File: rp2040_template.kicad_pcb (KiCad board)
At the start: 2 copper layers, 37 parts, among them J1 USB_C_Receptacle_USB2.0_14P, J3 SWD, SW1 SW_BOOT, SW2 SW_RESET, U1 RP2040, U2 W25Q16JVUXIQ TR, U3 AP2202K-3.3TRG1, Y1 ABM8-272-T3

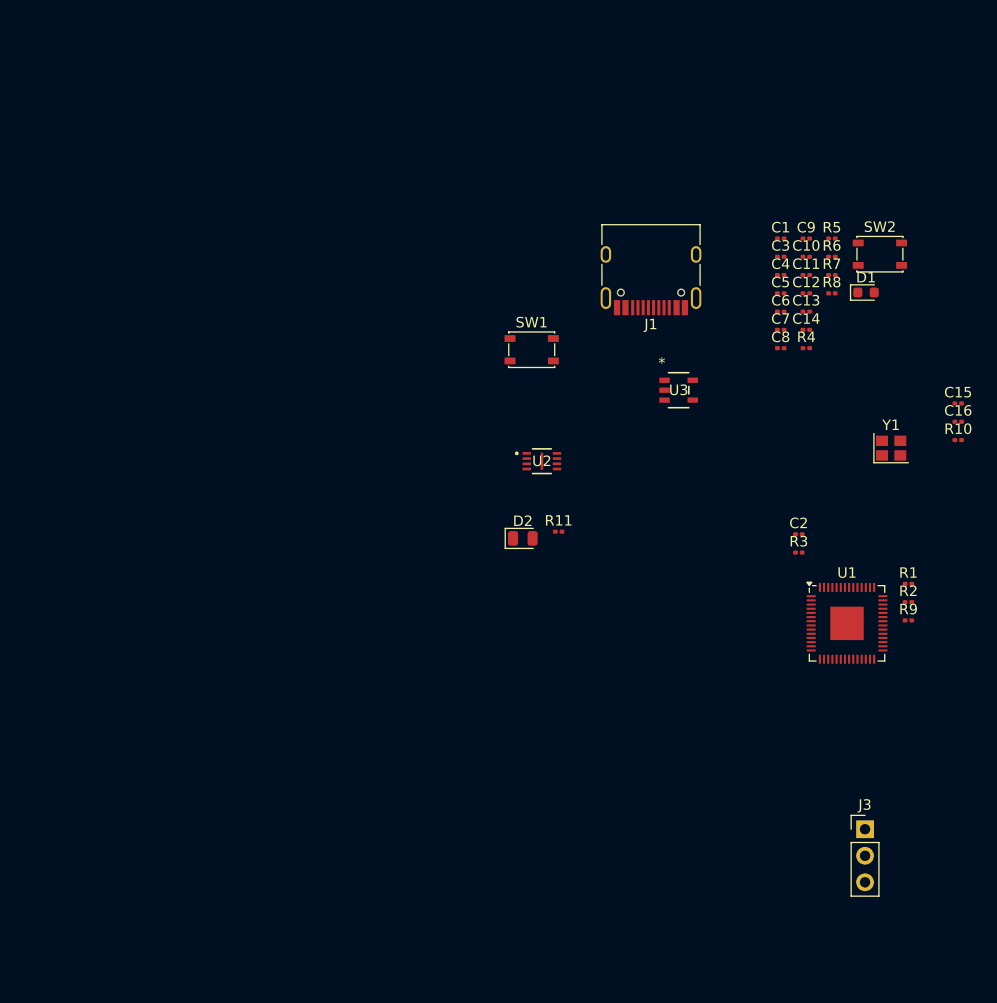
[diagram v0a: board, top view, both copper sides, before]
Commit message: Added castellated edges to PCB. began work on layout.
Signed-off-by: Nate <natelostintimeandspace@gmail.com>
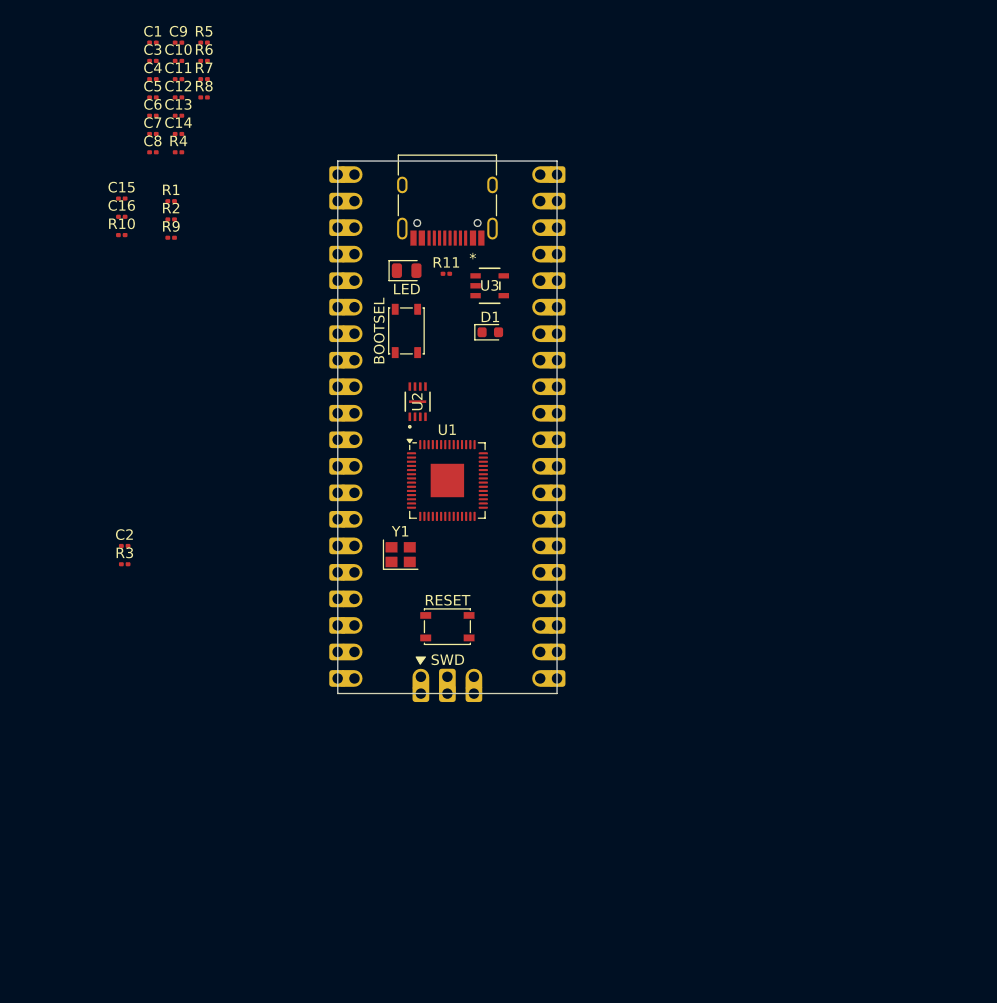
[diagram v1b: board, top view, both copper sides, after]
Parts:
- removed J3: SWD, Connector_PinHeader_2.54mm:PinHeader_1x03_P2.54mm_Vertical
- added REF**: castellated_tht_1x20, castellated:castellated_tht_1x20, F.Cu at (119.4, 51.3)
- added REF**: castellated_tht_1x20, castellated:castellated_tht_1x20, F.Cu at (101.6, 99.6)
- added REF**: castellated_tht_1x3, castellated:castellated_tht_1x3, F.Cu at (113.0, 99.4)
- moved C15 82.5 mm to (79.3, 53.6)
- moved C16 82.5 mm to (79.3, 55.3)
- moved R10 82.5 mm to (79.3, 57.1)
- moved R1 79.6 mm to (84.0, 53.8)
- moved R2 79.6 mm to (84.0, 55.6)
- moved R9 79.6 mm to (84.0, 57.3)
- moved C2 64.6 mm to (79.6, 86.9)
- moved R3 64.6 mm to (79.6, 88.6)
- moved C1 63.0 mm to (82.3, 38.7)
- moved C10 63.0 mm to (84.7, 40.4)
- moved C11 63.0 mm to (84.7, 42.2)
- moved C12 63.0 mm to (84.7, 43.9)
- moved C13 63.0 mm to (84.7, 45.7)
- moved C14 63.0 mm to (84.7, 47.4)
- moved C3 63.0 mm to (82.3, 40.4)
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- renumbered SW1 to BOOTSEL, D2 to LED, SW2 to RESET
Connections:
- U1 pad 24: /SWCLK -> unconnected-(U1-SWCLK-Pad24)
- U1 pad 25: /SWDIO -> unconnected-(U1-SWD-Pad25)
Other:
- board outline added: 21 x 51 mm

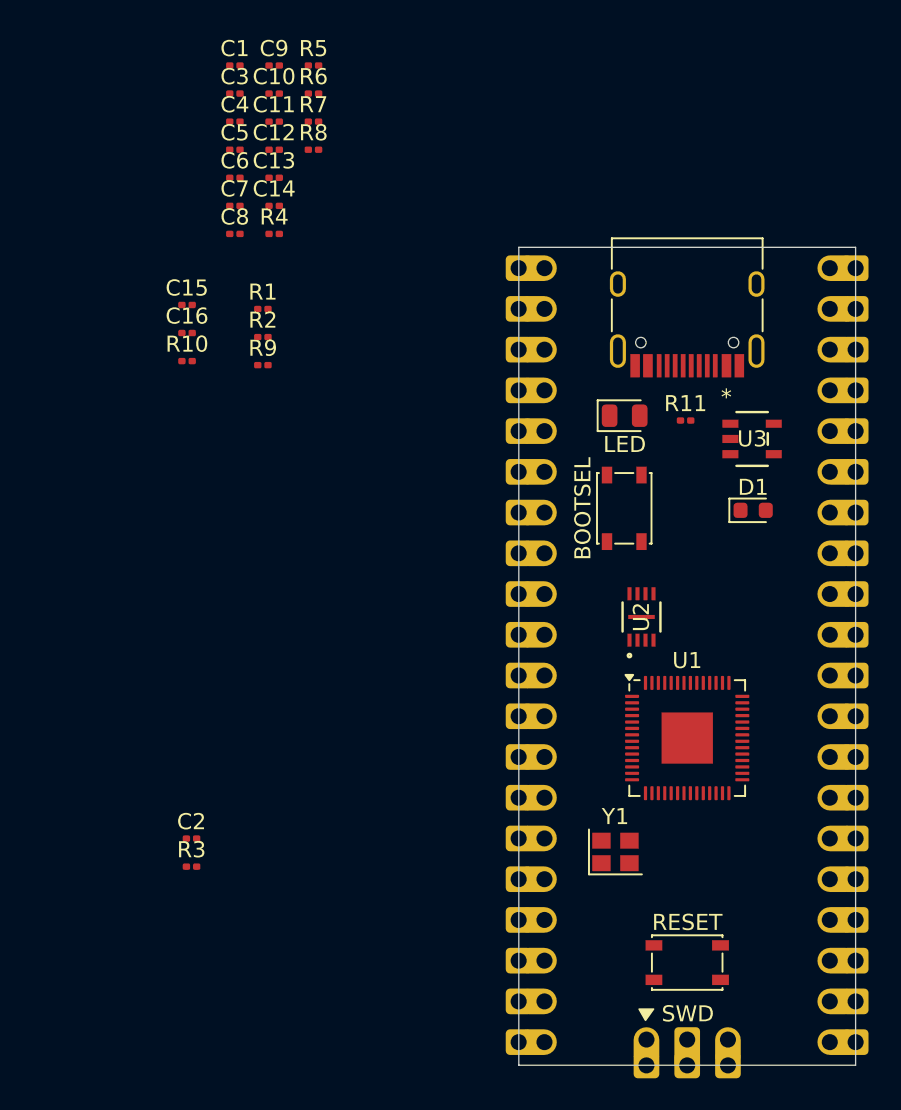
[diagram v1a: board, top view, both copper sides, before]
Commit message: Routed USB data, Oscillator, and began QSPI layout.
Signed-off-by: Nate <natelostintimeandspace@gmail.com>
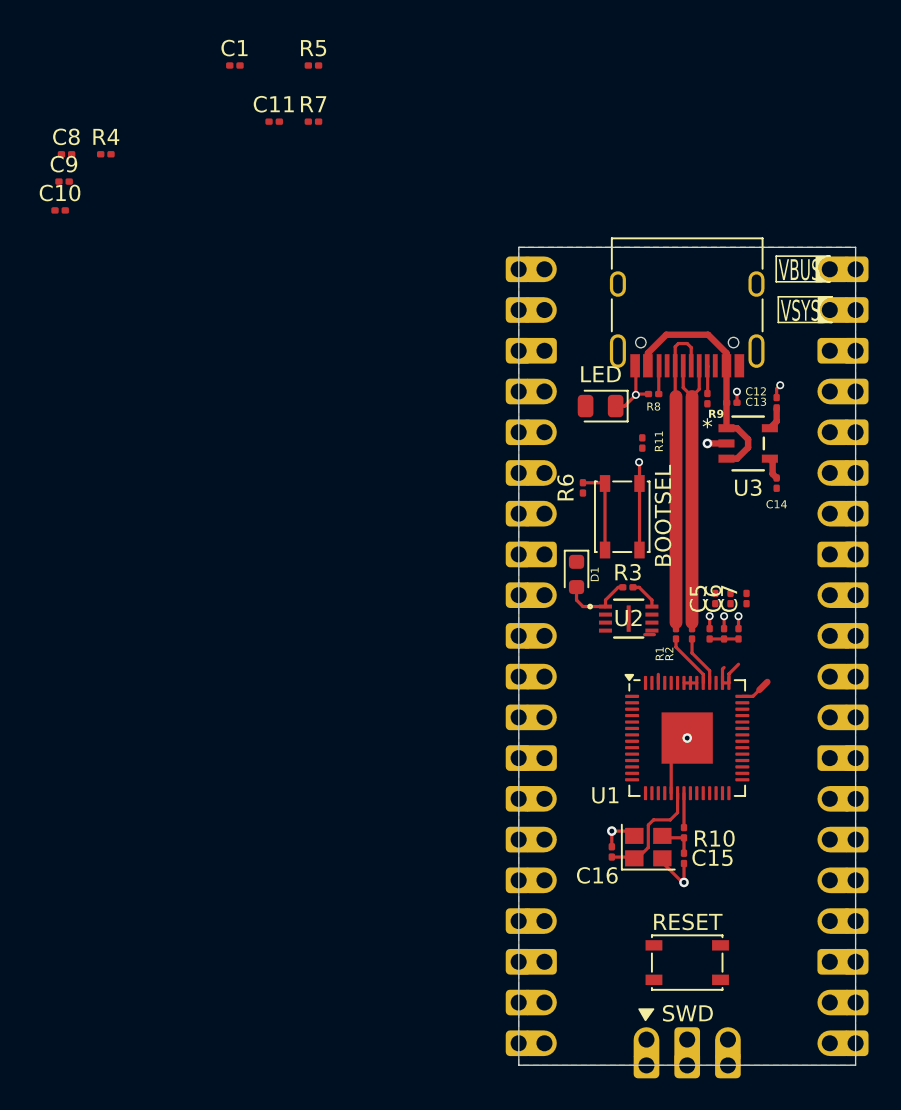
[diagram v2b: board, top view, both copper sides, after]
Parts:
- moved C15 46.4 mm to (110.3, 88.1), turned to 90 degrees
- moved C3 45.4 mm to (112.8, 74.1), turned to 90 degrees
- moved C4 44.8 mm to (113.7, 74.1), turned to 90 degrees
- moved R10 42.7 mm to (110.3, 86.5), turned to 90 degrees
- moved C16 41.8 mm to (105.8, 87.7), turned to -90 degrees
- moved C5 41.0 mm to (112.2, 71.9), turned to 90 degrees
- moved C6 40.5 mm to (113.2, 71.9), turned to 90 degrees
- moved C7 40.2 mm to (114.2, 71.9), turned to 90 degrees
- moved C14 35.8 mm to (116.1, 64.7), turned to -90 degrees
- moved C2 34.7 mm to (111.9, 74.1), turned to 90 degrees
- moved C13 34.3 mm to (116.1, 59.7), turned to 90 degrees
- moved R1 32.8 mm to (109.8, 74.1), turned to -90 degrees
- moved C12 32.6 mm to (113.3, 59.7)
- moved R2 32.5 mm to (110.8, 74.1), turned to -90 degrees
- moved R3 32.3 mm to (106.8, 71.2), turned to 180 degrees
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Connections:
- REF** pad 1: (no net) -> GND (x2)
- REF** pad 2: (no net) -> GND (x2)
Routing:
- net GND: track 0.00 -> 24.4 mm, vias 0 -> 11
- net USB_DP: track 0.00 -> 19.5 mm
- net USB_DM: track 0.00 -> 18.3 mm
- net VBUS: track 0.00 -> 15.1 mm
- net +3V3: track 0.00 -> 10.7 mm
- net /XIN: track 0.00 -> 7.35 mm
- net Net-(SW1-A): track 0.00 -> 5.54 mm
- net /~{QSPI_CS}: track 0.00 -> 4.59 mm
- net Net-(U1-USB_DP): track 0.00 -> 3.40 mm
- net Net-(U1-USB_DM): track 0.00 -> 3.15 mm
- net Net-(C15-Pad2): track 0.00 -> 2.36 mm
- net /XOUT: track 0.00 -> 2.14 mm
- net Net-(J1-CC1): track 0.00 -> 1.80 mm
- net Net-(J1-CC2): track 0.00 -> 1.78 mm
- net Net-(U3-BYP/ADJ): track 0.00 -> 1.38 mm
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- added copper zone on B.Cu, net GND
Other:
- board text added: "VBUS"
- board text added: "VSYS"

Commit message: Finished Rev A!
Signed-off-by: Nate <natelostintimeandspace@gmail.com>
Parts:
- removed the C2 at (111.9, 74.1)
- removed the REF** at (119.4, 51.4)
- removed the REF** at (101.6, 99.6)
- removed the REF** at (113.0, 99.4)
- removed U1: RP2040, Package_DFN_QFN:QFN-56-1EP_7x7mm_P0.4mm_EP3.2x3.2mm
- added ?: , , F.Cu at (147.5, 107.4)
- added ?: , , F.Cu at (146.2, 107.4)
- added ?: , , F.Cu at (147.5, 108.7)
- added ?: , , F.Cu at (148.8, 107.4)
- added ?: , , F.Cu at (146.2, 108.7)
- added ?: , , F.Cu at (148.8, 108.7)
- added ?: , , F.Cu at (147.5, 106.1)
- added ?: , , F.Cu at (146.2, 106.1)
- added ?: , , F.Cu at (148.8, 106.1)
- added C17: 100nF, Capacitor_SMD:C_01005_0402Metric, F.Cu at (152.4, 108.5)
- added C2: 100nF, Capacitor_SMD:C_0201_0603Metric, F.Cu at (152.4, 102.8)
- added C2: 100nF, Capacitor_SMD:C_01005_0402Metric, F.Cu at (146.7, 94.6)
- added D3: D_Schottky, Diode_SMD:Nexperia_CFP3_SOD-123W, F.Cu at (154.1, 79.6)
- added FID1: Fiducial, Fiducial:Fiducial_0.5mm_Mask1mm, F.Cu at (141.1, 78.0)
- added FID2: Fiducial, Fiducial:Fiducial_0.5mm_Mask1mm, F.Cu at (152.7, 125.8)
- added G***: LOGO, LOGO, B.Cu at (147.1, 120.7)
- added J2: Conn_01x20_Pin, castellated:castellated_tht_1x20, B.Cu at (138.6, 78.2)
- added J3: Conn_01x20_Pin, castellated:castellated_tht_1x20, F.Cu at (156.3, 78.2)
- added J4: Conn_01x03_Pin, castellated:castellated_tht_1x3, F.Cu at (150.0, 126.2)
- added REF**: OSHW-Logo2_7.3x6mm_SilkScreen, Symbol:OSHW-Logo2_7.3x6mm_SilkScreen, B.Cu at (145.7, 90.8)
- added U4: RP2040, Package_DFN_QFN:QFN-56-1EP_7x7mm_P0.4mm_EP3.2x3.2mm, F.Cu at (147.5, 107.4)
- C1, C10, C11, C12, C13, C14, C15, C16, C3, C4, C5, C6, C7, C8, C9: footprint Capacitor_SMD:C_0201_0603Metric -> Capacitor_SMD:C_01005_0402Metric
- D1: footprint Diode_SMD:D_0603_1608Metric -> Diode_SMD:D_01005_0402Metric
- LED1: renamed from LED; footprint LED_SMD:LED_0805_2012Metric -> LED_SMD:LED_0402_1005Metric_Pad0.77x0.64mm_HandSolder
- SW_1: renamed from BOOTSEL; value SW_BOOT -> BOOTSEL
- SW_2: renamed from RESET; value SW_RESET -> RESET
- U2: footprint footprints:USON-8_UX_2x3x0p6_WIN -> Package_SON:Winbond_USON-8-1EP_3x2mm_P0.5mm_EP0.2x1.6mm
- moved R7 96.9 mm to (150.4, 115.6)
- moved C10 95.6 mm to (150.6, 101.2), turned to 90 degrees
- moved C8 95.1 mm to (148.0, 101.1), turned to 90 degrees
- moved C9 94.4 mm to (142.4, 108.5), turned to 180 degrees
- moved C1 94.3 mm to (152.3, 101.9)
- moved C11 89.7 mm to (152.3, 101.2)
- moved R4 86.1 mm to (143.9, 94.9), turned to 180 degrees
- moved R5 79.1 mm to (143.9, 93.9)
- moved C5 54.7 mm to (147.7, 113.5), turned to -90 degrees
- moved C6 54.6 mm to (148.6, 113.5), turned to -90 degrees
- moved C13 49.3 mm to (151.7, 93.7), turned to -90 degrees
- moved Y1 48.8 mm to (145.9, 118.2)
- moved C16 48.7 mm to (145.5, 115.9), turned to 0 degrees
- moved R6 48.5 mm to (142.7, 94.2)
- moved R1 47.5 mm to (148.8, 101.2)
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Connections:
- C10 pad 1: Net-(U1-VREG_VOUT) -> +1V1
- C12 pad 1: VBUS -> /VSYS
- C6 pad 1: +3V3 -> +1V1
- C7 pad 1: +3V3 -> +1V1
- C8 pad 1: Net-(U1-VREG_VOUT) -> +3V3
- C9 pad 1: Net-(U1-VREG_VOUT) -> +3V3
- U3 pad 1: VBUS -> /VSYS
- U3 pad 3: VBUS -> /VSYS
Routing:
- net /GPIO0: track 0.00 -> 30.1 mm
- net /GPIO1: track 0.00 -> 28.5 mm
- net /USER_LED: track 0.00 -> 26.7 mm, vias 0 -> 2
- net /GPIO2: track 0.00 -> 23.8 mm
- net /RESET: track 0.00 -> 23.0 mm, vias 0 -> 2
- net +3V3: track 10.7 -> 33.2 mm, vias 0 -> 2
- net /GPIO3: track 0.00 -> 21.6 mm
- net /USER_SW: track 0.00 -> 21.3 mm, vias 0 -> 2
- net /GPIO15: track 0.00 -> 19.3 mm
- net /GPIO4: track 0.00 -> 19.3 mm
- net /GPIO16: track 0.00 -> 18.5 mm
- net /GPIO14: track 0.00 -> 17.7 mm
- net /ADC3: track 0.00 -> 17.6 mm
- net /SWCLK: track 0.00 -> 17.4 mm
- net /GPIO5: track 0.00 -> 17.3 mm
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- added copper zone on F.Cu, net +1V1
- added copper zone on F.Cu, net +3V3
- added copper zone on F.Cu, net /VSYS
- added copper zone on F.Cu, net GND
- added copper zone on F.Cu, net VBUS
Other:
- rule pad_to_mask_clearance: 0 -> 0.051
- board text added: "+3V3"
- board text added: "A0"
- board text added: "A1"
- board text added: "A2"
- board text added: "A3"
- board text added: "CLK"
- board text added: "DIO"
- board text added: "GND"
- board text added: "GP0"
- board text added: "GP1"
- board text added: "GP10"
- board text added: "GP11"
- board text added: "GP12"
- board text added: "GP13"
- board text added: "GP14"
- board text added: "GP15"
- board text added: "GP16"
- board text added: "GP17"
- board text added: "GP18"
- board text added: "GP19"
- board text added: "GP2"
- board text added: "GP20"
- board text added: "GP21"
- board text added: "GP22"
- board text added: "GP24"
- board text added: "GP3"
- board text added: "GP4"
- board text added: "GP5"
- board text added: "GP6"
- board text added: "GP7"
- board text added: "GP8"
- board text added: "GP9"
- board text added: "N.W. 2024 Rev A"
- board text added: "NC"
- board text added: "RP2040"
